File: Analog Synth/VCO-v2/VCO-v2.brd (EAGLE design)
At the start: 100 x 100 mm, 127 parts, among them IC1 TL084P, IC2 TL084P, IC3 78L09, IC4 78L05, IC5 79L09\, IC6 79L05, IC7 TL084P, Q1 J310, Q2 J310, Q3 2N3904, Q4 2N3904, Q5 2N3904, Q6 2N3906, T1 2N3904, T2 2N3904, T3 2N3904, T4 2N3904, T7 2N3904, U1 CA3096

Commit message: VCO-v2
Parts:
- CV-A-MAN: value 10k lin -> 100k lin
- renumbered FREQ-MAN to CV-A-MAN
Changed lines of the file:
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@@
 <element name="R6" library="resistor" package="0204/7" value="47k" x="58.42" y="96.52"/>
 <element name="VLT/OCT-A" library="pot" package="B64Y" value="10k trim" x="67.31" y="66.04"/>
-<element name="FREQ-MAN" library="pot" package="B64Y" value="10k lin" x="29.21" y="95.25"/>
+<element name="CV-A-MAN" library="pot" package="B64Y" value="100k lin" x="29.21" y="95.25"/>
 <element name="R11" library="resistor" package="0204/7" value="22k" x="85.09" y="64.77" rot="R90"/>
 <element name="R12" library="resistor" package="0204/7" value="1k" x="85.09" y="69.85" rot="R90"/>
@@
 <signal name="N$1">
 <contactref element="CV-A" pad="P$3"/>
-<contactref element="FREQ-MAN" pad="S"/>
+<contactref element="CV-A-MAN" pad="S"/>
 <wire x1="17.78" y1="96.52" x2="29.21" y2="95.25" width="0" layer="19" extent="1-1"/>
 </signal>
@@
 </signal>
 <signal name="+5V">
-<contactref element="FREQ-MAN" pad="A"/>
+<contactref element="CV-A-MAN" pad="A"/>
 <contactref element="U1" pad="10"/>
 <contactref element="U1" pad="13"/>
@@
 </signal>
 <signal name="-5V">
-<contactref element="FREQ-MAN" pad="E"/>
+<contactref element="CV-A-MAN" pad="E"/>
 <contactref element="IC1" pad="12"/>
 <contactref element="R14" pad="1"/>

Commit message: fixed error in VCO-v2 schematic - CV sum had a tuner going to -5 V instead of -9 V
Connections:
- net -5V: no longer R14.1
- net -9V: now also R14.1
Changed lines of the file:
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@@
 <contactref element="CV-A-MAN" pad="E"/>
 <contactref element="IC1" pad="12"/>
-<contactref element="R14" pad="1"/>
 <contactref element="U1" pad="5"/>
 <contactref element="U1" pad="8"/>
@@
 <contactref element="PWM-MAN" pad="E"/>
 <wire x1="87.63" y1="72.39" x2="88.9" y2="84.455" width="0" layer="19" extent="1-1"/>
-<wire x1="85.09" y1="71.12" x2="87.63" y2="72.39" width="0" layer="19" extent="1-1"/>
-<wire x1="68.58" y1="74.93" x2="85.09" y2="71.12" width="0" layer="19" extent="1-1"/>
+<wire x1="68.58" y1="74.93" x2="87.63" y2="72.39" width="0" layer="19" extent="1-1"/>
 <wire x1="67.31" y1="82.55" x2="68.58" y2="74.93" width="0" layer="19" extent="1-1"/>
 <wire x1="71.12" y1="96.52" x2="67.31" y2="82.55" width="0" layer="19" extent="1-1"/>
-<wire x1="74.93" y1="54.61" x2="85.09" y2="71.12" width="0" layer="19" extent="1-1"/>
+<wire x1="74.93" y1="54.61" x2="68.58" y2="74.93" width="0" layer="19" extent="1-1"/>
 <wire x1="74.93" y1="49.53" x2="74.93" y2="54.61" width="0" layer="19" extent="1-1"/>
 <wire x1="71.12" y1="44.45" x2="74.93" y2="49.53" width="0" layer="19" extent="1-1"/>
@@
 <contactref element="C20" pad="1"/>
 <contactref element="R42" pad="2"/>
+<contactref element="R14" pad="1"/>
 <wire x1="73.66" y1="78.74" x2="73.66" y2="82.55" width="0" layer="19" extent="1-1"/>
+<wire x1="85.09" y1="71.12" x2="73.66" y2="78.74" width="0" layer="19" extent="1-1"/>
 <wire x1="27.94" y1="52.07" x2="73.66" y2="78.74" width="0" layer="19" extent="1-1"/>
 <wire x1="16.002" y1="57.15" x2="27.94" y2="52.07" width="0" layer="19" extent="1-1"/>

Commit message: VCO-v2 - increased size of resistors around the triangle-wave x2 gain stage
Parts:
- R30, R31: value 10k -> 100k
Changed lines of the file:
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@@
 <element name="C20" library="resistor" package="C025-050X050" value="0.1u" x="27.94" y="50.8" rot="R270"/>
 <element name="C21" library="resistor" package="C025-050X050" value="0.1u" x="27.94" y="59.69" rot="R270"/>
-<element name="R30" library="resistor" package="0204/7" value="10k" x="29.21" y="81.28"/>
-<element name="R31" library="resistor" package="0204/7" value="10k" x="27.94" y="77.47"/>
+<element name="R30" library="resistor" package="0204/7" value="100k" x="29.21" y="81.28"/>
+<element name="R31" library="resistor" package="0204/7" value="100k" x="27.94" y="77.47"/>
 <element name="TRIANGLE" library="!synth_sch" package="MONO_JACK" value="I/O" x="27.94" y="73.66"/>
 <element name="R32" library="resistor" package="0204/7" value="1k" x="38.1" y="85.09" rot="R180"/>

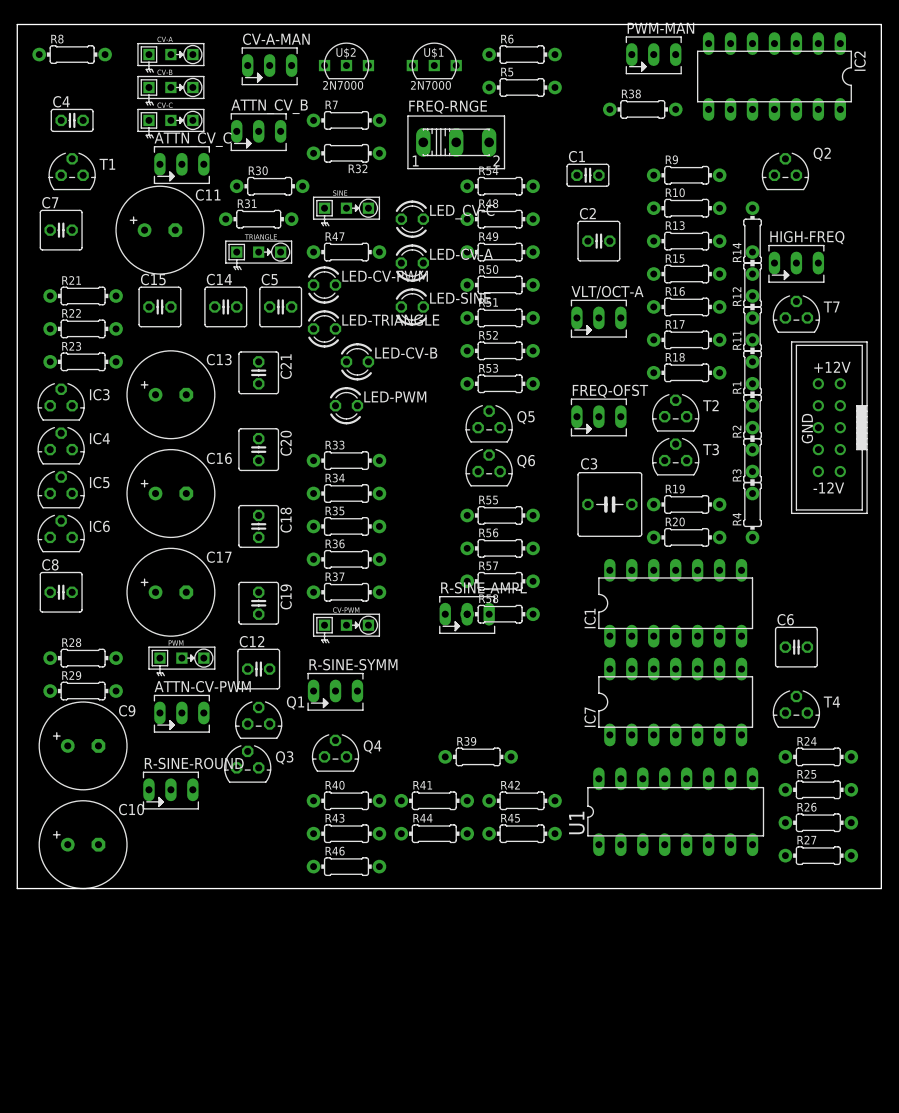
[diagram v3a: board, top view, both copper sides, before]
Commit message: VCO-v2 improved readability
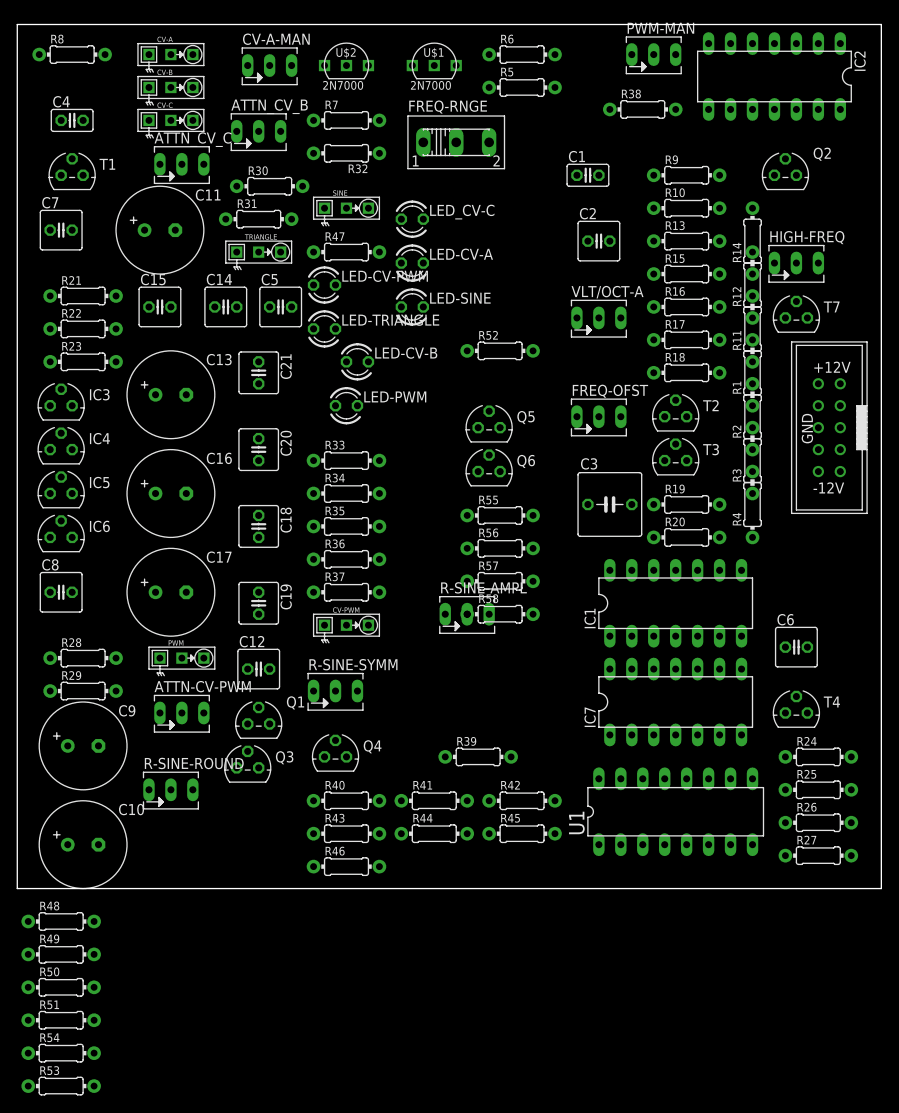
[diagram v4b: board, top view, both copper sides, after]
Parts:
- moved R54 112.5 mm to (5.08, -19.1)
- moved R48 95.8 mm to (5.08, -3.81)
- moved R49 95.8 mm to (5.08, -7.62)
- moved R50 95.8 mm to (5.08, -11.4)
- moved R51 95.8 mm to (5.08, -15.2)
- moved R53 95.8 mm to (5.08, -22.9)
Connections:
- removed net N$36 (its old number): C21.1
- removed net N$57: LED_CV-C.K, R50.1
- removed net N$58: LED-CV-PWM.A, Q5.3
- removed net N$59: LED-PWM.K, R48.1
- removed net N$60: LED-TRIANGLE.K, R49.1
- new net N$61: LED_CV-C.K, R49.1
- new net N$62: LED-TRIANGLE.K, R50.1
- new net N$63: LED-PWM.K, R51.1
- new net N$7: LED-CV-PWM.A, R53.1
- net -12V: now also C10.-; no longer C10.+
- net -5V: now also C16.-, C21.1; no longer C16.+
- net -9V: now also C13.-; no longer C13.+
- net CV-PWM: now also LED-CV-PWM.K; no longer R53.2
- net GND: now also C10.+, C13.+, C16.+; no longer C10.-, C13.-, C16.-
- net N$11: now also Q5.3, R53.2; no longer LED-CV-PWM.K, R53.1
- net N$56: now also R48.1; no longer R51.1

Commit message: VCO-v2.2 - updated an LED resistor value and exported PDF
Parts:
- R51: value 4.7k -> 8.2k
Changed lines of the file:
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@@
 <element name="R49" library="resistor" package="0204/7" value="4.7k" x="5.08" y="-7.62"/>
 <element name="R50" library="resistor" package="0204/7" value="4.7k" x="5.08" y="-11.43"/>
-<element name="R51" library="resistor" package="0204/7" value="4.7k" x="5.08" y="-15.24"/>
+<element name="R51" library="resistor" package="0204/7" value="8.2k" x="5.08" y="-15.24"/>
 <element name="R54" library="resistor" package="0204/7" value="4.7k" x="5.08" y="-19.05"/>
 <element name="R53" library="resistor" package="0204/7" value="4.7k" x="5.08" y="-22.86"/>

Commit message: CBS - Cigar Box Sequencer - 8 step - starting to put together a schematic for it
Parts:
- moved R48 76.1 mm to (47.0, 59.7)
- moved R49 76.1 mm to (47.0, 55.9)
- moved R50 76.1 mm to (47.0, 52.1)
- moved R51 76.1 mm to (47.0, 48.3)
- moved R53 76.1 mm to (47.0, 40.6)
- moved R54 76.1 mm to (47.0, 44.5)
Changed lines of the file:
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@@
 <element name="R57" library="resistor" package="0204/7" value="47k" x="55.88" y="35.56"/>
 <element name="R58" library="resistor" package="0204/7" value="33k" x="55.88" y="31.75"/>
-<element name="R48" library="resistor" package="0204/7" value="4.7k" x="5.08" y="-3.81"/>
-<element name="R49" library="resistor" package="0204/7" value="4.7k" x="5.08" y="-7.62"/>
-<element name="R50" library="resistor" package="0204/7" value="4.7k" x="5.08" y="-11.43"/>
-<element name="R51" library="resistor" package="0204/7" value="8.2k" x="5.08" y="-15.24"/>
-<element name="R54" library="resistor" package="0204/7" value="4.7k" x="5.08" y="-19.05"/>
-<element name="R53" library="resistor" package="0204/7" value="4.7k" x="5.08" y="-22.86"/>
+<element name="R48" library="resistor" package="0204/7" value="4.7k" x="46.99" y="59.69"/>
+<element name="R49" library="resistor" package="0204/7" value="4.7k" x="46.99" y="55.88"/>
+<element name="R50" library="resistor" package="0204/7" value="4.7k" x="46.99" y="52.07"/>
+<element name="R51" library="resistor" package="0204/7" value="8.2k" x="46.99" y="48.26"/>
+<element name="R54" library="resistor" package="0204/7" value="4.7k" x="46.99" y="44.45"/>
+<element name="R53" library="resistor" package="0204/7" value="4.7k" x="46.99" y="40.64"/>
 </elements>
 <signals>
@@
 <contactref element="LED_CV-C" pad="K"/>
 <contactref element="R49" pad="1"/>
-<wire x1="1.27" y1="-7.62" x2="46.99" y2="77.47" width="0" layer="19" extent="1-1"/>
+<wire x1="43.18" y1="55.88" x2="46.99" y2="77.47" width="0" layer="19" extent="1-1"/>
 </signal>
 <signal name="N$62">
 <contactref element="LED-TRIANGLE" pad="K"/>
 <contactref element="R50" pad="1"/>
-<wire x1="1.27" y1="-11.43" x2="36.83" y2="64.77" width="0" layer="19" extent="1-1"/>
+<wire x1="43.18" y1="52.07" x2="36.83" y2="64.77" width="0" layer="19" extent="1-1"/>
 </signal>
 <signal name="N$63">
 <contactref element="LED-PWM" pad="K"/>
 <contactref element="R51" pad="1"/>
-<wire x1="1.27" y1="-15.24" x2="39.37" y2="55.88" width="0" layer="19" extent="1-1"/>
+<wire x1="43.18" y1="48.26" x2="39.37" y2="55.88" width="0" layer="19" extent="1-1"/>
 </signal>
 <signal name="N$64">
 <contactref element="LED-SINE" pad="K"/>
 <contactref element="R54" pad="1"/>
-<wire x1="1.27" y1="-19.05" x2="46.99" y2="67.31" width="0" layer="19" extent="1-1"/>
+<wire x1="43.18" y1="44.45" x2="46.99" y2="67.31" width="0" layer="19" extent="1-1"/>
 </signal>
 <signal name="N$36">
@@
 <contactref element="R50" pad="2"/>
 <contactref element="R51" pad="2"/>
-<wire x1="53.34" y1="48.26" x2="59.69" y2="62.23" width="0" layer="19" extent="1-1"/>
-<wire x1="8.89" y1="-3.81" x2="53.34" y2="48.26" width="0" layer="19" extent="1-1"/>
-<wire x1="8.89" y1="-7.62" x2="8.89" y2="-3.81" width="0" layer="19" extent="1-1"/>
-<wire x1="8.89" y1="-11.43" x2="8.89" y2="-7.62" width="0" layer="19" extent="1-1"/>
-<wire x1="8.89" y1="-15.24" x2="8.89" y2="-11.43" width="0" layer="19" extent="1-1"/>
-<wire x1="8.89" y1="-19.05" x2="8.89" y2="-15.24" width="0" layer="19" extent="1-1"/>
+<wire x1="50.8" y1="59.69" x2="59.69" y2="62.23" width="0" layer="19" extent="1-1"/>
+<wire x1="50.8" y1="55.88" x2="50.8" y2="59.69" width="0" layer="19" extent="1-1"/>
+<wire x1="50.8" y1="52.07" x2="50.8" y2="55.88" width="0" layer="19" extent="1-1"/>
+<wire x1="50.8" y1="48.26" x2="50.8" y2="52.07" width="0" layer="19" extent="1-1"/>
+<wire x1="53.34" y1="48.26" x2="50.8" y2="48.26" width="0" layer="19" extent="1-1"/>
+<wire x1="50.8" y1="44.45" x2="50.8" y2="48.26" width="0" layer="19" extent="1-1"/>
 </signal>
 <signal name="N$56">
 <contactref element="R48" pad="1"/>
 <contactref element="LED-CV-B" pad="K"/>
-<wire x1="1.27" y1="-3.81" x2="40.64" y2="60.96" width="0" layer="19" extent="1-1"/>
+<wire x1="40.64" y1="60.96" x2="43.18" y2="59.69" width="0" layer="19" extent="1-1"/>
 </signal>
 <signal name="N$7">
 <contactref element="R53" pad="1"/>
 <contactref element="LED-CV-PWM" pad="A"/>
-<wire x1="1.27" y1="-22.86" x2="34.29" y2="69.85" width="0" layer="19" extent="1-1"/>
+<wire x1="43.18" y1="40.64" x2="34.29" y2="69.85" width="0" layer="19" extent="1-1"/>
 </signal>
 <signal name="N$11">
 <contactref element="R53" pad="2"/>
 <contactref element="Q5" pad="3"/>
-<wire x1="8.89" y1="-22.86" x2="53.34" y2="53.34" width="0" layer="19" extent="1-1"/>
+<wire x1="50.8" y1="40.64" x2="53.34" y2="53.34" width="0" layer="19" extent="1-1"/>
 </signal>
 </signals>
